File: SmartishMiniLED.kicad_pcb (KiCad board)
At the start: 2 copper layers, 30 x 60 mm, 35 parts, among them J1 USB_C_Receptacle_USB2.0, J2 BUTTON, J3 Screw_Terminal_01x03, J4 Conn_01x02, P1 NeopixelStripPads, P2 NeopixelStripPads, Q1 MMBT2222, Q2 MMBT2222, Q3 IRLML6344, Q4 IRF7410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

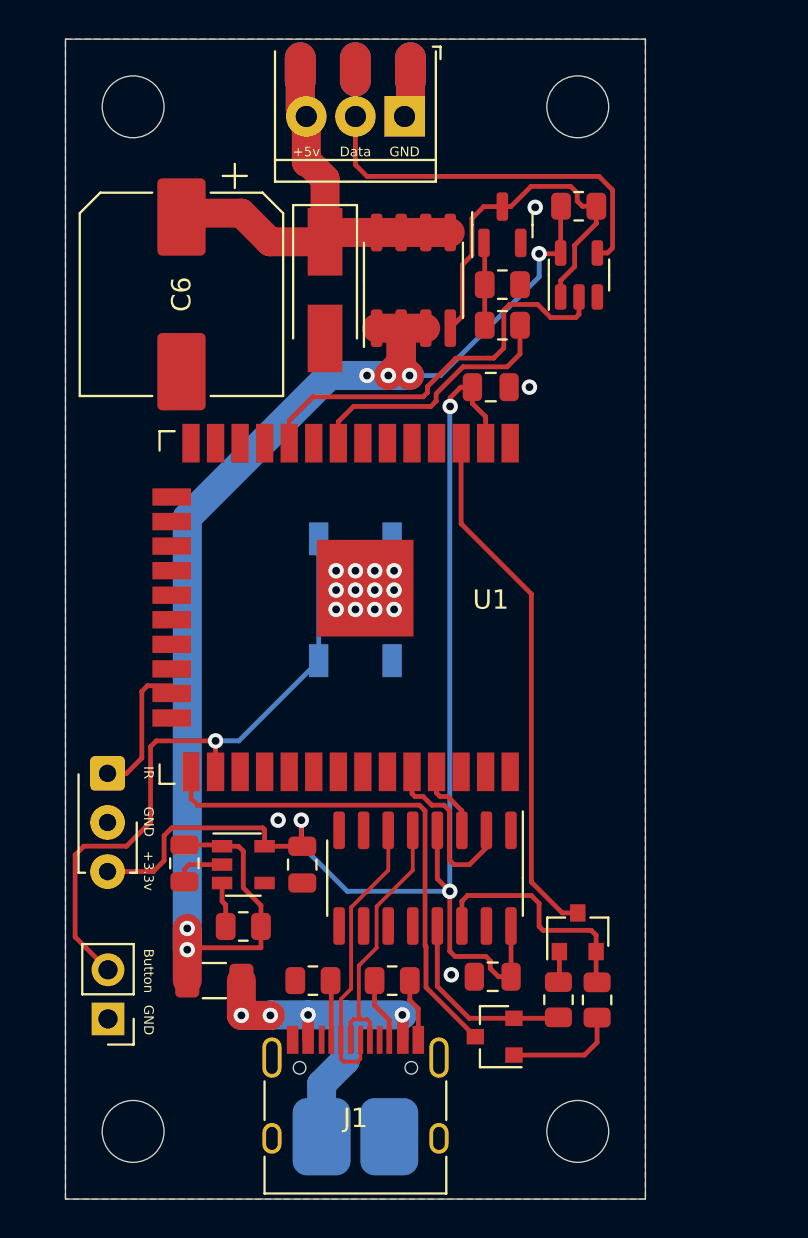
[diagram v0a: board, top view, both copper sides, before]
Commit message: Various fixes
- Moved the capacitor to the other side of the MOSFET to fix brownout issues, fixes #4
- Added extra components needed to fix restart when programming via USB, fixes #2
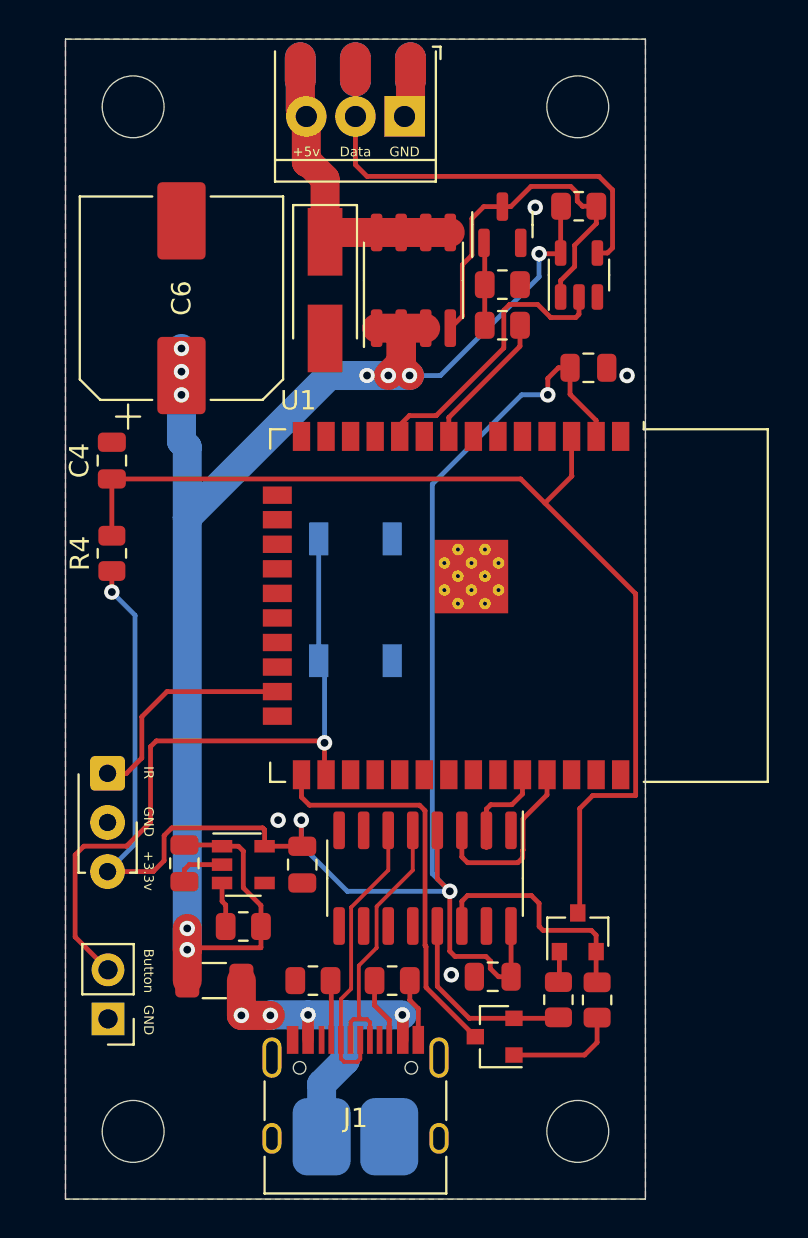
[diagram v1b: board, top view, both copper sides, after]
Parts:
- added C4: 1uF, Capacitor_SMD:C_0805_2012Metric, F.Cu at (138.4, 77.8)
- added R4: 10K, Resistor_SMD:R_0805_2012Metric, F.Cu at (138.4, 82.6)
- U1: footprint RF_Module:ESP32-WROOM-32 -> RF_Module:ESP32-WROOM-32D
- moved U1 5.72 mm to (156.5, 85.3)
- moved C5 5.15 mm to (163.1, 73.0)
- moved C6 0.20 mm to (142.0, 69.4), turned to 90 degrees
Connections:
- C6 pad 1: VBUS -> +5V
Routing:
- net /RESET: track 27.7 -> 55.6 mm
- net +3V3: track 66.7 -> 88.9 mm, vias 3 -> 4
- net +5V: track 73.2 -> 82.1 mm, vias 6 -> 9
- net VBUS: track 25.2 -> 17.2 mm
- net /GPIO0: track 26.9 -> 20.6 mm
- net /LED_POWER: track 13.3 -> 7.28 mm
- net /NEOPIXEL: track 20.8 -> 14.8 mm
- net /TXD0: track 4.20 -> 9.57 mm
- net /IR: track 7.22 -> 11.8 mm
- net /RXD0: track 9.66 -> 5.19 mm
- net /BUTTON: track 33.6 -> 36.7 mm
- net GND: vias 16 -> 4

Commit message: Adding some power LEDs to help diagnose power issues.
Also various fixes to checks.
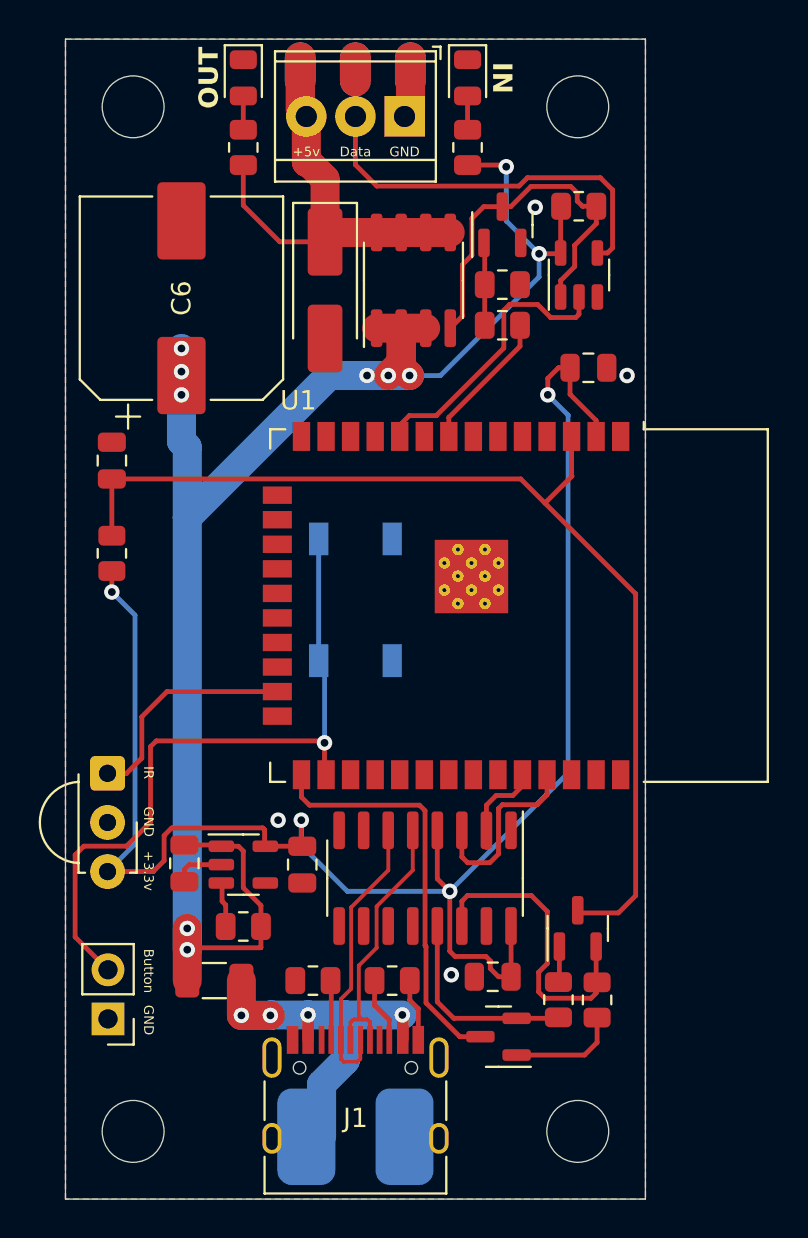
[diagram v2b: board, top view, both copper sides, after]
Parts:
- added D2: LED, LED_SMD:LED_0805_2012Metric, F.Cu at (145.2, 58.0)
- added D3: LED, LED_SMD:LED_0805_2012Metric, F.Cu at (156.8, 58.0)
- added R10: R, Resistor_SMD:R_0805_2012Metric, F.Cu at (145.2, 61.6)
- added R11: R, Resistor_SMD:R_0805_2012Metric, F.Cu at (156.8, 61.6)
- moved Q1 0.20 mm to (158.4, 107.6)
- moved Q2 0.20 mm to (162.5, 102.0)
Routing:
- net +5V: track 82.1 -> 89.3 mm, vias 9 -> 10
- net VBUS: track 17.2 -> 24.3 mm
- net /RTS: track 12.3 -> 16.0 mm
- net Net-(D3-A): track 0.00 -> 1.75 mm
- net Net-(D2-A): track 0.00 -> 1.75 mm
- net +3V3: track 88.9 -> 88.2 mm
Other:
- board text added: "IN"
- board text added: "OUT"

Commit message: DRC fixes
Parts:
- moved J3 0.80 mm to (153.5, 60.8)
- moved C6 0.60 mm to (142.0, 70.0)
- moved D1 0.42 mm to (149.4, 69.4)
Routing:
- net +5V: track 89.3 -> 87.7 mm
